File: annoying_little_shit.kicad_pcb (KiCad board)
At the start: 2 copper layers, 33 x 23 mm, 15 parts, among them J1 Conn_01x06_Pin, Q1 Si2319CDS, Q2 MMBT3904, U1 ATtiny13V-10SU

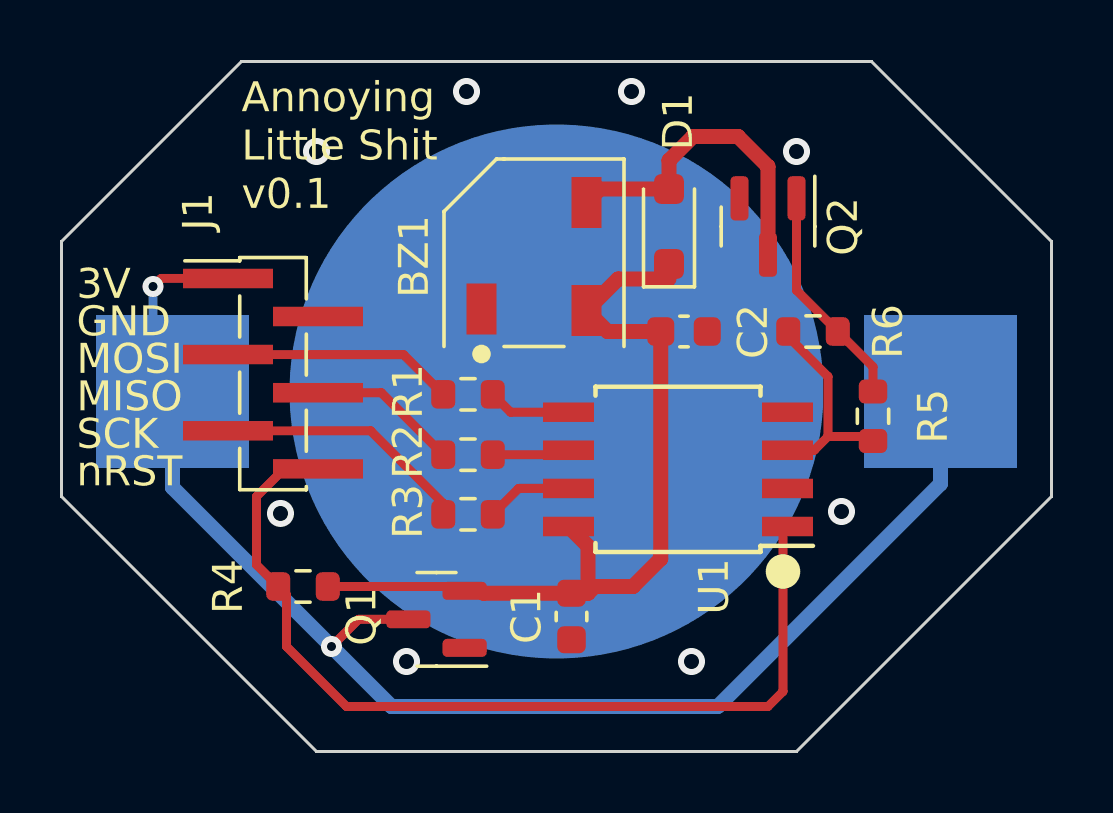
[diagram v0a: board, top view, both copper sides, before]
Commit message: Version 1.0: Current limiting resistor on buzzer, larger footprint for buzzer to make it easier to solder, remove pull-up on nRST to limit current drain (there should also be an internal one on the AVR
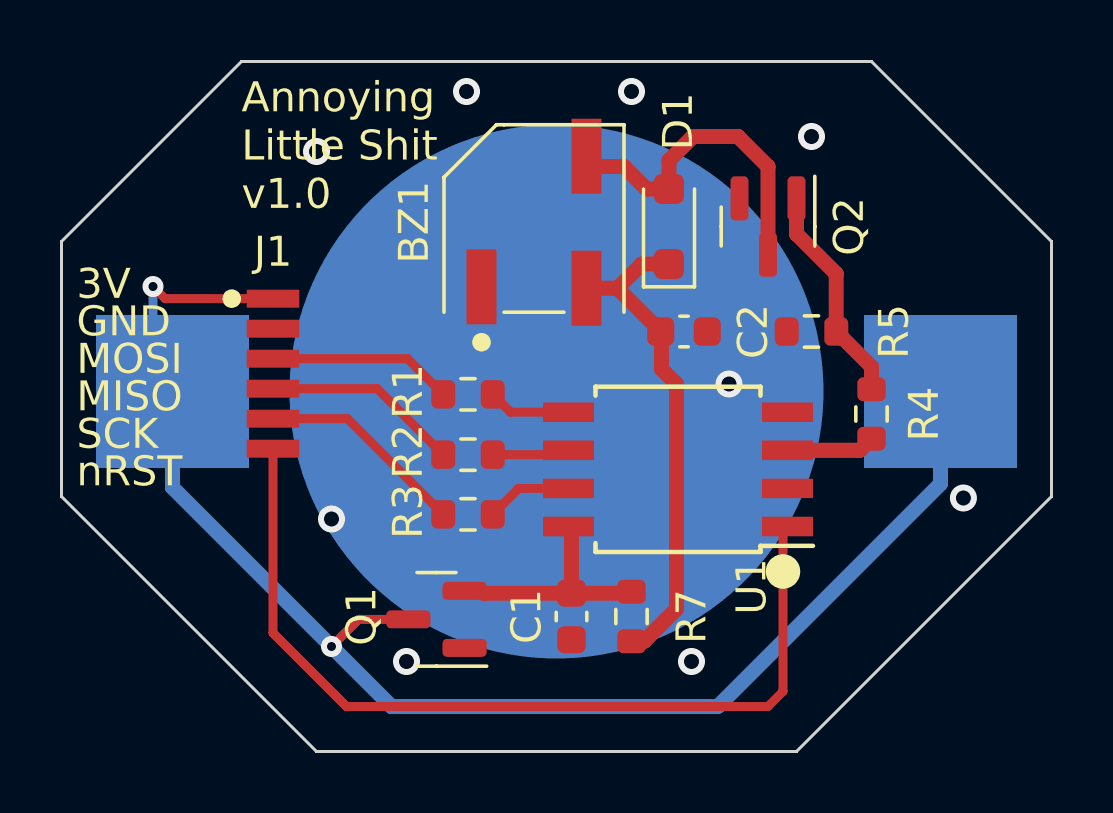
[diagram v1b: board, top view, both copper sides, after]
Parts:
- removed the R4 at (122.5, 69.0)
- removed R6: 330R, Resistor_SMD:R_0603_1608Metric
- added R5: 10K, Resistor_SMD:R_0603_1608Metric, F.Cu at (139.5, 60.5)
- added R7: 27R, Resistor_SMD:R_0603_1608Metric, F.Cu at (133.5, 70.0)
- J1: footprint Connector_PinHeader_1.27mm:PinHeader_1x06_P1.27mm_Vertical_SMD_Pin1Left -> als_footprints:PinHeader_1x06_P1.00mm_Vertical_SMD_Aligned
- moved BZ1 1.14 mm to (130.2, 56.9)
- moved R4 0.09 mm to (141.5, 63.2)
- renumbered R5 to R4
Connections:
- BZ1 pad 2: +3V0 -> Net-(BZ1-+)
- C2 pad 1: +3V0 -> Net-(BZ1-+)
- D1 pad 1: +3V0 -> Net-(BZ1-+)
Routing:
- net +3V0: track 27.7 -> 7.54 mm
- net Net-(BZ1-+): track 0.00 -> 16.5 mm
- net Net-(U1-PB4): track 7.15 -> 2.96 mm
- net Net-(J1-Pin_4): track 5.03 -> 6.59 mm
- net Net-(J1-Pin_3): track 7.72 -> 6.17 mm
- net Net-(J1-Pin_6): track 31.0 -> 29.9 mm
- net Net-(BT1-+): track 48.3 -> 49.4 mm
- net Net-(J1-Pin_5): track 8.04 -> 7.00 mm
- net GND: vias 8 -> 9
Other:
- board text added: "Annoying Little Shit v1.0"
- board text removed: "Annoying Little Shit v0.1"
